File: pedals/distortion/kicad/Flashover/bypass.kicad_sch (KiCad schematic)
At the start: 13 parts, among them K1 G6K-2F-Y 5VDC, Q1 MMBT3904

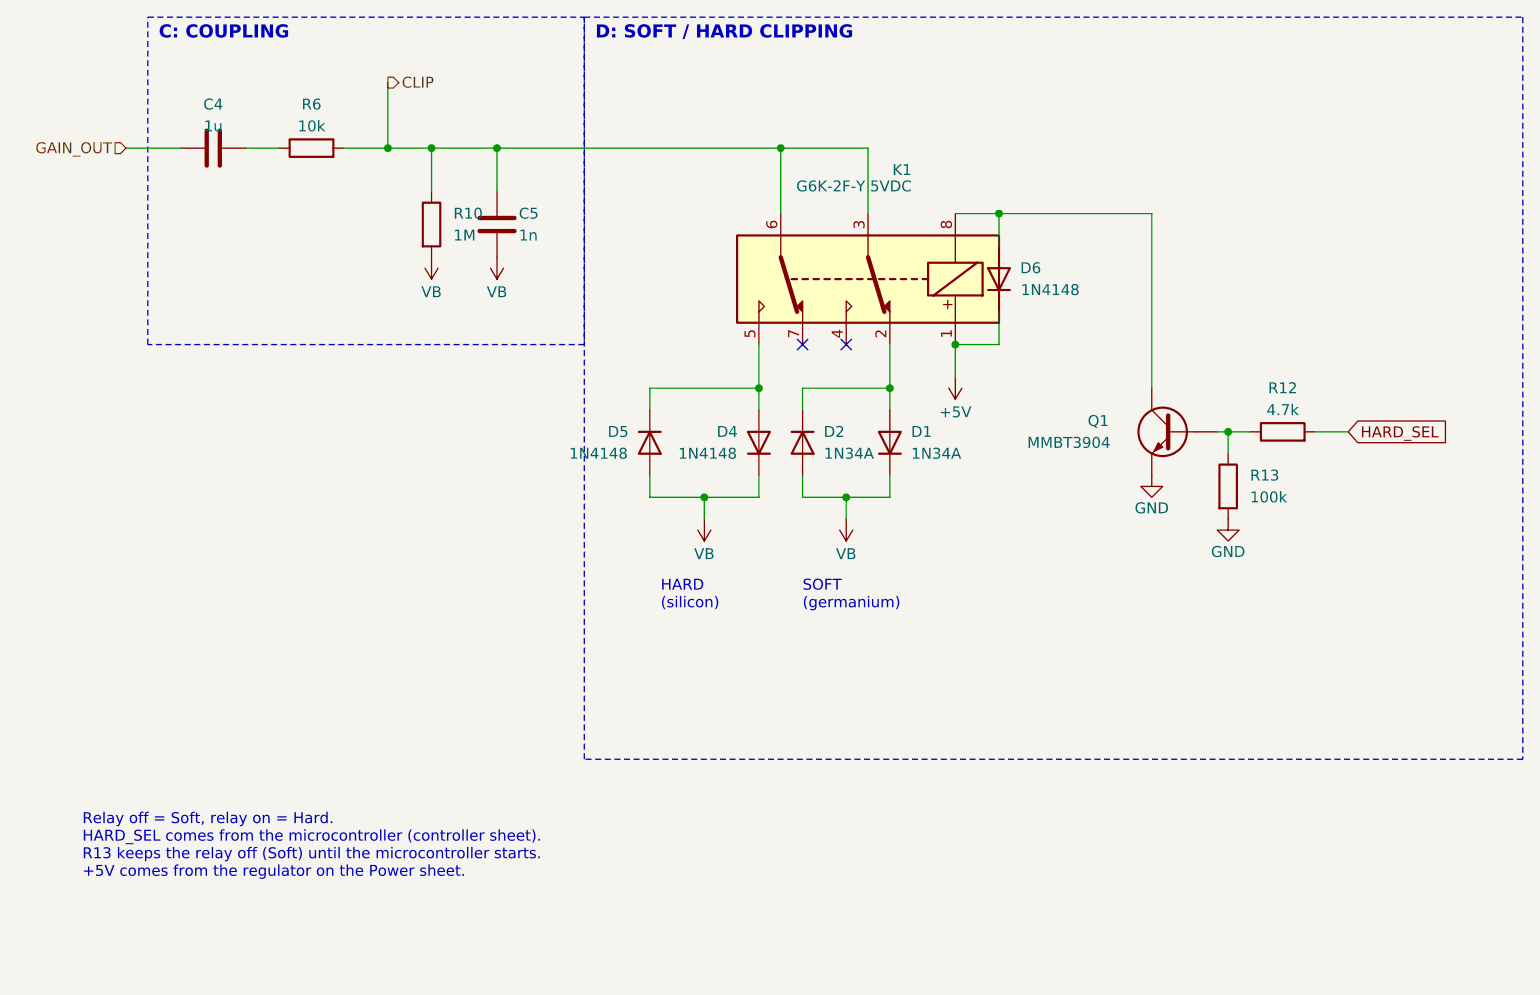
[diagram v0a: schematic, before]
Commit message: Add Flashover bypass sheet; complete schematic
Bypass sheet: fail-safe G6K-2 relay bypass (NC contacts join the jacks
when unpowered), input/output jacks moved here from the audio sheets
(now FX_IN/FX_OUT), relay driver on FX_ON, soft-touch footswitch and
Link LED. Relay coils on K1 and K2 now take +5V on pin 1 (marked +).
Root sheet laid out in four columns. ERC clean.

Co-Authored-By: Claude Opus 5.5 <noreply@anthropic.com>
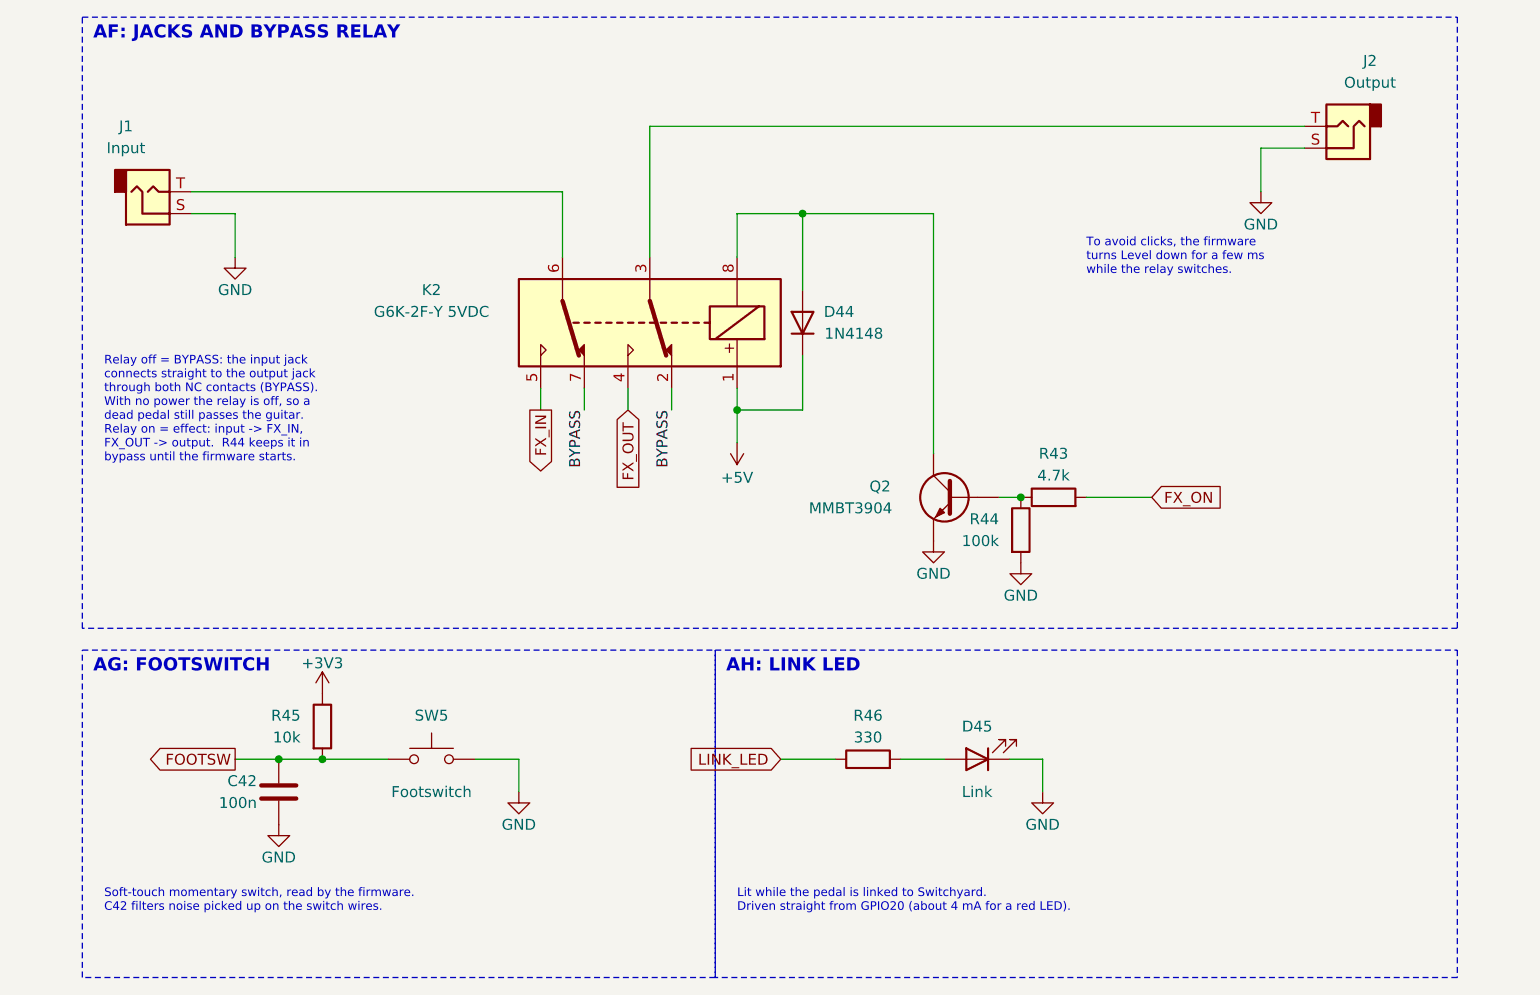
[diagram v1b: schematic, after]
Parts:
- removed C4: 1u, symbol Device:C
- removed C5: 1n, symbol Device:C
- removed D1, D2: 1N34A, symbol Device:D
- removed D4, D5, D6: 1N4148, symbol Device:D
- removed K1: G6K-2F-Y 5VDC, symbol Relay:G6K-2
- removed Q1: MMBT3904, symbol Device:Q_NPN
- removed R10: 1M, symbol Device:R
- removed R12: 4.7k, symbol Device:R
- removed R13: 100k, symbol Device:R
- removed R6: 10k, symbol Device:R
- added C42: 100n, symbol Device:C
- added D44: 1N4148, symbol Device:D
- added D45: Link, symbol Device:LED
- added J1: Input, symbol Connector_Audio:AudioJack2
- added J2: Output, symbol Connector_Audio:AudioJack2
- added K2: G6K-2F-Y 5VDC, symbol Relay:G6K-2
- added Q2: MMBT3904, symbol Device:Q_NPN
- added R43: 4.7k, symbol Device:R
- added R44: 100k, symbol Device:R
- added R45: 10k, symbol Device:R
- added R46: 330, symbol Device:R
- added SW5: Footswitch, symbol Switch:SW_Push
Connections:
- net +5V: now also D44.1 (K), K2.1
- net GND: now also C42.2, D45.1 (K), J1.S, J2.S, Q2.E, R44.2, SW5.2
- new net: Q2.B, R43.1, R44.1
- new net: D44.2 (A), K2.8, Q2.C
- new net: J2.T, K2.3
- new net: J1.T, K2.6
- new net: D45.2 (A), R46.2
- new net +3V3: R45.1
- new net BYPASS: K2.2, K2.7
- new net FOOTSW: C42.1, R45.2, SW5.1
- new net FX_IN: K2.5
- new net FX_ON: R43.2
- new net FX_OUT: K2.4
- new net LINK_LED: R46.1
- no-connect marks 2 -> 0
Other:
- note added: "AF: JACKS AND BYPASS RELAY"
- note added: "AG: FOOTSWITCH"
- note added: "AH: LINK LED"
- note added: "Lit while the pedal is linked to Switchyard. Driven straight from GPIO20 (about 4 mA for a red LED)."
- note added: "Relay off = BYPASS: the input jack connects straight to the output jack through both NC contacts (BYPASS). With no power the relay is off, so a dead pedal still passes the guitar. Relay on = effect: input -> FX_IN, FX_OUT -> output. R44 keeps it in bypass until the firmware starts."
- note added: "Soft-touch momentary switch, read by the firmware. C42 filters noise picked up on the switch wires."
- note added: "To avoid clicks, the firmware turns Level down for a few ms while the relay switches."
- note removed: "C: COUPLING"
- note removed: "D: SOFT / HARD CLIPPING"
- note removed: "HARD (silicon)"
- note removed: "Relay off = Soft, relay on = Hard. HARD_SEL comes from the microcontroller (controller sheet). R13 keeps the relay off (Soft) until the microcontroller starts. +5V comes from the regulator on the Power sheet."
- note removed: "SOFT (germanium)"
- title: Flashover - Clipping -> Flashover - Bypass

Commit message: Assign Flashover footprints
Surface-mount for assembly; through-hole for jacks, encoders, panel LEDs,
the Soft/Hard button, the TO-220 regulator and the germanium diodes.
Q1/Q2 use the MMBT3904 symbol, 1N4148 -> 1N4148W, 1N5817 -> SS14.

Co-Authored-By: Claude Opus 5.5 <noreply@anthropic.com>
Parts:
- removed Q2: MMBT3904, symbol Device:Q_NPN
- added Q2: MMBT3904, Package_TO_SOT_SMD:SOT-23, symbol Transistor_BJT:MMBT3904
- C42: footprint (none) -> Capacitor_SMD:C_0805_2012Metric
- D44: value 1N4148 -> 1N4148W; footprint (none) -> Diode_SMD:D_SOD-123
- D45: footprint (none) -> LED_THT:LED_D3.0mm
- J1, J2: footprint (none) -> Connector_Audio:Jack_6.35mm_Neutrik_NRJ4HF_Horizontal
- K2: footprint (none) -> Relay_SMD:Relay_DPDT_Omron_G6K-2F-Y
- R43, R44, R45, R46: footprint (none) -> Resistor_SMD:R_0805_2012Metric
- SW5: footprint (none) -> Connector_JST:JST_PH_B2B-PH-K_1x02_P2.00mm_Vertical
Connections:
- net GND: now also Q2.2 (E)
- net at R43.1, R44.1: now also Q2.1 (B)
- net at D44.2 (A), K2.8: now also Q2.3 (C)
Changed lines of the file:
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@@
 			(effects (font (size 1.27 1.27)))
 		)
-		(property "Footprint" ""
+		(property "Footprint" "Connector_Audio:Jack_6.35mm_Neutrik_NRJ4HF_Horizontal"
 			(at 27.94 73.66 0)
 			(hide yes)
@@
 		(instances
 			(project "Flashover"
-				(path "/d341370c-bf24-48b8-b9fb-db9600491445/8db23f6e-d1ef-4344-be69-b3d596abd399"
+				(path "/872055d3-e01a-4a82-8c05-28c93674a700/d9140471-6418-4b11-add1-2e36f8b5b006"
 					(reference "J1")
 					(unit 1)
@@
 		(instances
 			(project "Flashover"
-				(path "/d341370c-bf24-48b8-b9fb-db9600491445/8db23f6e-d1ef-4344-be69-b3d596abd399"
+				(path "/872055d3-e01a-4a82-8c05-28c93674a700/d9140471-6418-4b11-add1-2e36f8b5b006"
 					(reference "#PWR122")
 					(unit 1)
@@
 			(effects (font (size 1.27 1.27)))
 		)
-		(property "Footprint" ""
+		(property "Footprint" "Connector_Audio:Jack_6.35mm_Neutrik_NRJ4HF_Horizontal"
 			(at 167.64 66.04 0)
 			(hide yes)
@@
 		(instances
 			(project "Flashover"
-				(path "/d341370c-bf24-48b8-b9fb-db9600491445/8db23f6e-d1ef-4344-be69-b3d596abd399"
+				(path "/872055d3-e01a-4a82-8c05-28c93674a700/d9140471-6418-4b11-add1-2e36f8b5b006"
 					(reference "J2")
 					(unit 1)
@@
 		(instances
 			(project "Flashover"
-				(path "/d341370c-bf24-48b8-b9fb-db9600491445/8db23f6e-d1ef-4344-be69-b3d596abd399"
+				(path "/872055d3-e01a-4a82-8c05-28c93674a700/d9140471-6418-4b11-add1-2e36f8b5b006"
 					(reference "#PWR123")
 					(unit 1)
@@
 			(effects (font (size 1.27 1.27)))
 		)
-		(property "Footprint" ""
+		(property "Footprint" "Relay_SMD:Relay_DPDT_Omron_G6K-2F-Y"
 			(at 86.36 88.9 0)
 			(hide yes)
@@
 		(instances
 			(project "Flashover"
-				(path "/d341370c-bf24-48b8-b9fb-db9600491445/8db23f6e-d1ef-4344-be69-b3d596abd399"
+				(path "/872055d3-e01a-4a82-8c05-28c93674a700/d9140471-6418-4b11-add1-2e36f8b5b006"
 					(reference "K2")
 					(unit 1)
@@
 	)
 	(symbol
-		(lib_id "Device:Q_NPN")
+		(lib_id "Transistor_BJT:MMBT3904")
 		(at 121.92 109.22 0)
 		(mirror y)
@@
 			(effects (font (size 1.27 1.27)))
 		)
-		(property "Footprint" ""
+		(property "Footprint" "Package_TO_SOT_SMD:SOT-23"
 			(at 121.92 109.22 0)
 			(hide yes)
@@
 			(effects (font (size 1.27 1.27)))
 		)
-		(pin "B"
-		)
-		(pin "C"
-		)
-		(pin "E"
-		)
-		(instances
-			(project "Flashover"
-				(path "/d341370c-bf24-48b8-b9fb-db9600491445/8db23f6e-d1ef-4344-be69-b3d596abd399"
+		(pin "1"
+		)
+		(pin "2"
+		)
+		(pin "3"
+		)
+		(instances
+			(project "Flashover"
+				(path "/872055d3-e01a-4a82-8c05-28c93674a700/d9140471-6418-4b11-add1-2e36f8b5b006"
 					(reference "Q2")
 					(unit 1)
@@
 			(effects (font (size 1.27 1.27)))
 		)
-		(property "Value" "1N4148"
-			(at 110.109 90.17 90)
-			(show_name no)
-			(do_not_autoplace no)
-			(effects (font (size 1.27 1.27)))
-		)
-		(property "Footprint" ""
+		(property "Value" "1N4148W"
+			(at 110.6805 90.17 90)
+			(show_name no)
+			(do_not_autoplace no)
+			(effects (font (size 1.27 1.27)))
+		)
+		(property "Footprint" "Diode_SMD:D_SOD-123"
 			(at 104.14 88.9 90)
 			(hide yes)
@@
 		(instances
 			(project "Flashover"
-				(path "/d341370c-bf24-48b8-b9fb-db9600491445/8db23f6e-d1ef-4344-be69-b3d596abd399"
+				(path "/872055d3-e01a-4a82-8c05-28c93674a700/d9140471-6418-4b11-add1-2e36f8b5b006"
 					(reference "D44")
 					(unit 1)
@@
 		(instances
 			(project "Flashover"
-				(path "/d341370c-bf24-48b8-b9fb-db9600491445/8db23f6e-d1ef-4344-be69-b3d596abd399"
+				(path "/872055d3-e01a-4a82-8c05-28c93674a700/d9140471-6418-4b11-add1-2e36f8b5b006"
 					(reference "#PWR124")
 					(unit 1)
@@
 		(instances
 			(project "Flashover"
-				(path "/d341370c-bf24-48b8-b9fb-db9600491445/8db23f6e-d1ef-4344-be69-b3d596abd399"
+				(path "/872055d3-e01a-4a82-8c05-28c93674a700/d9140471-6418-4b11-add1-2e36f8b5b006"
 					(reference "#PWR125")
 					(unit 1)
@@
 			(effects (font (size 1.27 1.27)))
 		)
-		(property "Footprint" ""
+		(property "Footprint" "Resistor_SMD:R_0805_2012Metric"
 			(at 133.35 109.22 90)
 			(hide yes)
@@
 		(instances
 			(project "Flashover"
-				(path "/d341370c-bf24-48b8-b9fb-db9600491445/8db23f6e-d1ef-4344-be69-b3d596abd399"
+				(path "/872055d3-e01a-4a82-8c05-28c93674a700/d9140471-6418-4b11-add1-2e36f8b5b006"
 					(reference "R43")
 					(unit 1)
@@
 			(effects (font (size 1.27 1.27)) (justify right))
 		)
-		(property "Footprint" ""
+		(property "Footprint" "Resistor_SMD:R_0805_2012Metric"
 			(at 129.54 113.03 0)
 			(hide yes)
@@
 		(instances
 			(project "Flashover"
-				(path "/d341370c-bf24-48b8-b9fb-db9600491445/8db23f6e-d1ef-4344-be69-b3d596abd399"
+				(path "/872055d3-e01a-4a82-8c05-28c93674a700/d9140471-6418-4b11-add1-2e36f8b5b006"
 					(reference "R44")
 					(unit 1)
@@
 		(instances
 			(project "Flashover"
-				(path "/d341370c-bf24-48b8-b9fb-db9600491445/8db23f6e-d1ef-4344-be69-b3d596abd399"
+				(path "/872055d3-e01a-4a82-8c05-28c93674a700/d9140471-6418-4b11-add1-2e36f8b5b006"
 					(reference "#PWR126")
 					(unit 1)
@@
 			(effects (font (size 1.27 1.27)))
 		)
-		(property "Footprint" ""
+		(property "Footprint" "Connector_JST:JST_PH_B2B-PH-K_1x02_P2.00mm_Vertical"
 			(at 60.96 139.7 0)
 			(hide yes)
@@
 		(instances
 			(project "Flashover"
-				(path "/d341370c-bf24-48b8-b9fb-db9600491445/8db23f6e-d1ef-4344-be69-b3d596abd399"
+				(path "/872055d3-e01a-4a82-8c05-28c93674a700/d9140471-6418-4b11-add1-2e36f8b5b006"
 					(reference "SW5")
 					(unit 1)
@@
 			(effects (font (size 1.27 1.27)) (justify right))
 		)
-		(property "Footprint" ""
+		(property "Footprint" "Resistor_SMD:R_0805_2012Metric"
 			(at 48.26 135.89 0)
 			(hide yes)
@@
 		(instances
 			(project "Flashover"
-				(path "/d341370c-bf24-48b8-b9fb-db9600491445/8db23f6e-d1ef-4344-be69-b3d596abd399"
+				(path "/872055d3-e01a-4a82-8c05-28c93674a700/d9140471-6418-4b11-add1-2e36f8b5b006"
 					(reference "R45")
 					(unit 1)
@@
 		(instances
 			(project "Flashover"
-				(path "/d341370c-bf24-48b8-b9fb-db9600491445/8db23f6e-d1ef-4344-be69-b3d596abd399"
+				(path "/872055d3-e01a-4a82-8c05-28c93674a700/d9140471-6418-4b11-add1-2e36f8b5b006"
 					(reference "#PWR127")
 					(unit 1)
@@
 			(effects (font (size 1.27 1.27)) (justify right))
 		)
-		(property "Footprint" ""
+		(property "Footprint" "Capacitor_SMD:C_0805_2012Metric"
 			(at 43.18 143.51 0)
 			(hide yes)
@@
 		(instances
 			(project "Flashover"
-				(path "/d341370c-bf24-48b8-b9fb-db9600491445/8db23f6e-d1ef-4344-be69-b3d596abd399"
+				(path "/872055d3-e01a-4a82-8c05-28c93674a700/d9140471-6418-4b11-add1-2e36f8b5b006"
 					(reference "C42")
 					(unit 1)
@@
 		(instances
 			(project "Flashover"
-				(path "/d341370c-bf24-48b8-b9fb-db9600491445/8db23f6e-d1ef-4344-be69-b3d596abd399"
+				(path "/872055d3-e01a-4a82-8c05-28c93674a700/d9140471-6418-4b11-add1-2e36f8b5b006"
 					(reference "#PWR128")
 					(unit 1)
@@
 		(instances
 			(project "Flashover"
-				(path "/d341370c-bf24-48b8-b9fb-db9600491445/8db23f6e-d1ef-4344-be69-b3d596abd399"
+				(path "/872055d3-e01a-4a82-8c05-28c93674a700/d9140471-6418-4b11-add1-2e36f8b5b006"
 					(reference "#PWR129")
 					(unit 1)
@@
 			(effects (font (size 1.27 1.27)))
 		)
-		(property "Footprint" ""
+		(property "Footprint" "Resistor_SMD:R_0805_2012Metric"
 			(at 111.76 139.7 90)
 			(hide yes)
@@
 		(instances
 			(project "Flashover"
-				(path "/d341370c-bf24-48b8-b9fb-db9600491445/8db23f6e-d1ef-4344-be69-b3d596abd399"
+				(path "/872055d3-e01a-4a82-8c05-28c93674a700/d9140471-6418-4b11-add1-2e36f8b5b006"
 					(reference "R46")
 					(unit 1)
@@
 			(effects (font (size 1.27 1.27)))
 		)
-		(property "Footprint" ""
+		(property "Footprint" "LED_THT:LED_D3.0mm"
 			(at 124.46 139.7 0)
 			(hide yes)
@@
 		(instances
 			(project "Flashover"
-				(path "/d341370c-bf24-48b8-b9fb-db9600491445/8db23f6e-d1ef-4344-be69-b3d596abd399"
+				(path "/872055d3-e01a-4a82-8c05-28c93674a700/d9140471-6418-4b11-add1-2e36f8b5b006"
 					(reference "D45")
 					(unit 1)
@@
 		(instances
 			(project "Flashover"
-				(path "/d341370c-bf24-48b8-b9fb-db9600491445/8db23f6e-d1ef-4344-be69-b3d596abd399"
+				(path "/872055d3-e01a-4a82-8c05-28c93674a700/d9140471-6418-4b11-add1-2e36f8b5b006"
 					(reference "#PWR130")
 					(unit 1)

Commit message: Split Flashover into main and control boards; place parts
Main board (Flashover): audio, controller, pots, MIDI, bypass and the five
top-mounted jacks.  Control board (Flashover_Controls): encoders, LED rings,
LED driver, Soft/Hard button and panel LEDs.  J7/J8 2x10 board connector,
M3 mounting holes, regulator laid flat.  Placement only, not yet routed.

Co-Authored-By: Claude Opus 5.5 <noreply@anthropic.com>
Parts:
- removed D45: Link, LED_THT:LED_D3.0mm, symbol Device:LED
- removed R46: 330, Resistor_SMD:R_0805_2012Metric, symbol Device:R
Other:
- note added: "Soft-touch momentary switch on the panel, wired to a 2-pin JST PH connector. Read by the firmware; C42 filters noise picked up on the switch wires."
- note removed: "AH: LINK LED"
- note removed: "Lit while the pedal is linked to Switchyard. Driven straight from GPIO20 (about 4 mA for a red LED)."
- note removed: "Soft-touch momentary switch, read by the firmware. C42 filters noise picked up on the switch wires."

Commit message: Use a side-entry footswitch connector on the Flashover main board
The upright JST PH header (SW5) sat under the control board with only
5 mm above it for the wires. The side-entry S2B-PH-K-S takes the plug
from the front edge, so it can be connected after stacking. It moves
2.75 mm toward the edge, and the FOOTSW track is shortened to match.
Still 0 unconnected, 0 errors, schematic parity clean.

Co-Authored-By: Claude Opus 5.5 <noreply@anthropic.com>
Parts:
- SW5: footprint Connector_JST:JST_PH_B2B-PH-K_1x02_P2.00mm_Vertical -> Connector_JST:JST_PH_S2B-PH-K_1x02_P2.00mm_Horizontal
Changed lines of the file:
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@@
 			(effects (font (size 1.27 1.27)))
 		)
-		(property "Footprint" "Connector_JST:JST_PH_B2B-PH-K_1x02_P2.00mm_Vertical"
+		(property "Footprint" "Connector_JST:JST_PH_S2B-PH-K_1x02_P2.00mm_Horizontal"
 			(at 60.96 139.7 0)
 			(hide yes)
